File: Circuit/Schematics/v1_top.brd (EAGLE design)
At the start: 31.5 x 31.5 mm, 42 parts, among them IC1 LM2936MP-3.3, X2 16 Mhz, X3 16 Mhz

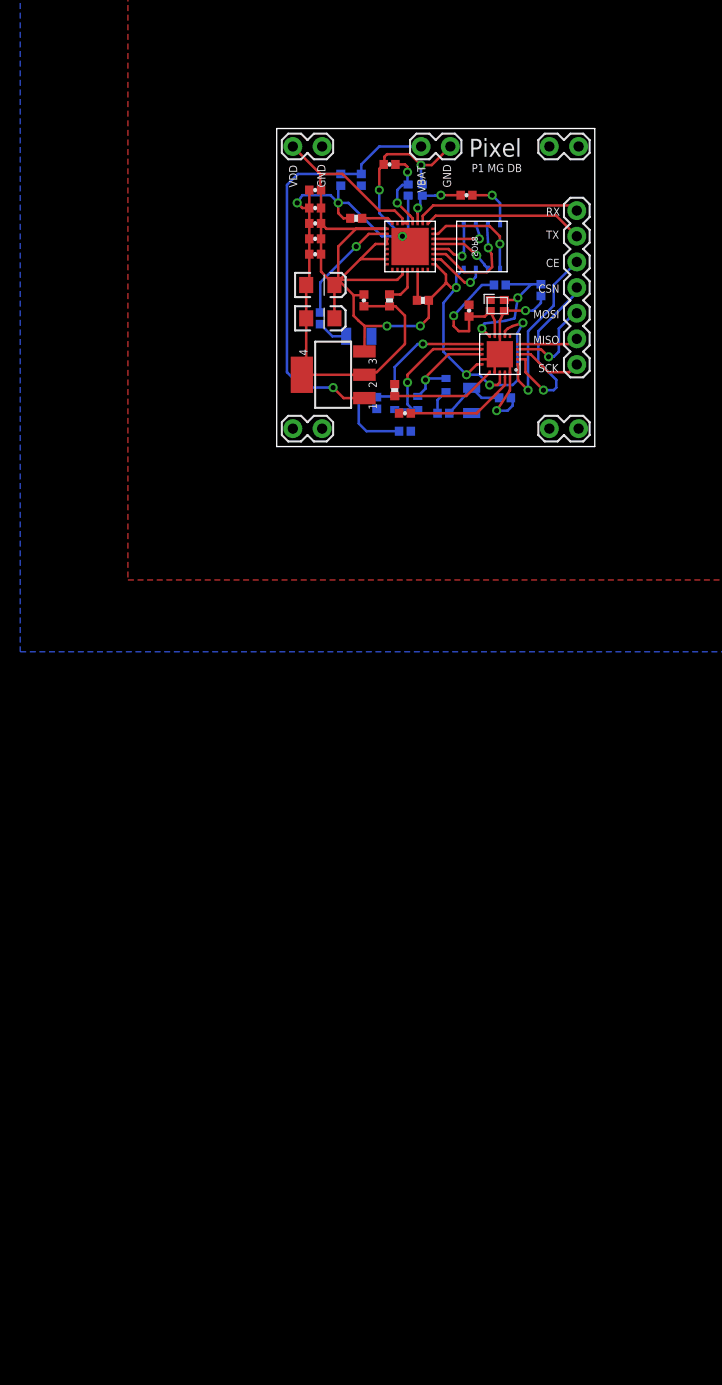
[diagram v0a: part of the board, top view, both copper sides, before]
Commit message: Teensy board designed, redesigning system components board and making hardware components consistent
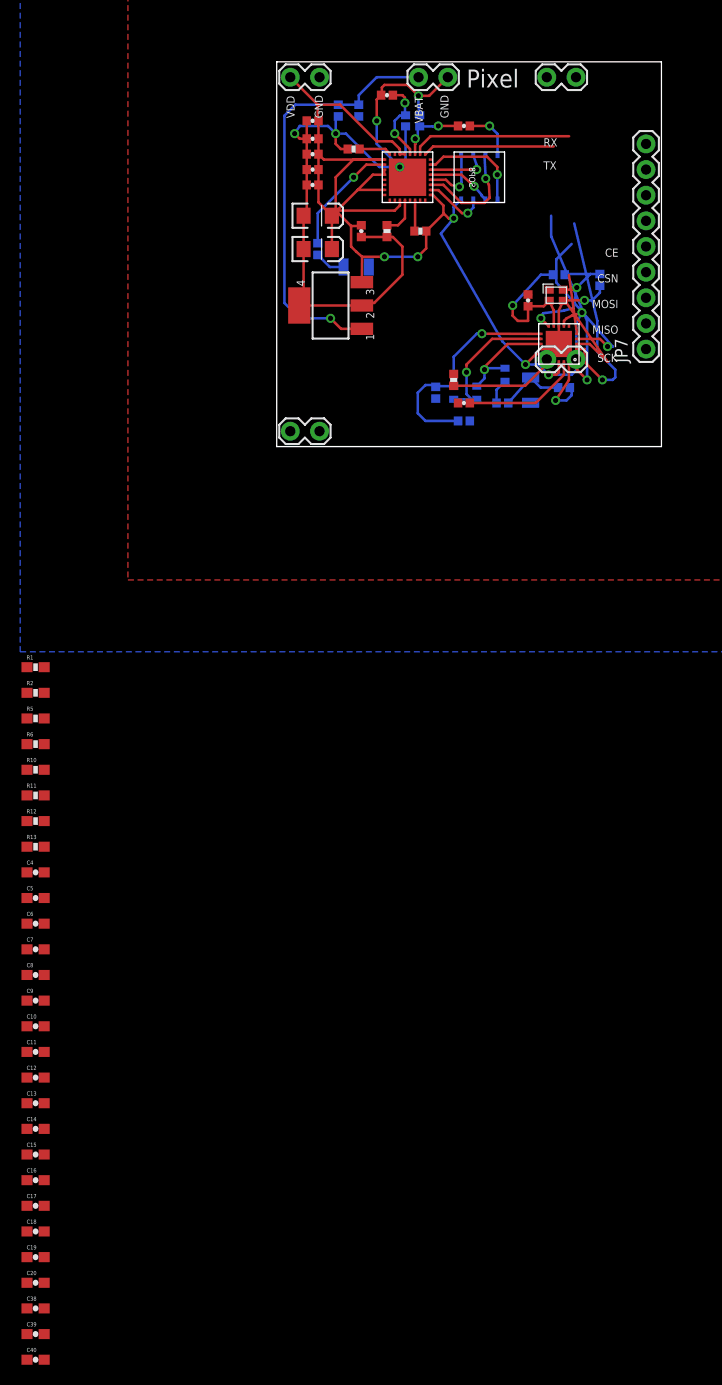
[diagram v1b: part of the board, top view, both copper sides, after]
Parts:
- removed JP1: (no value), SparkFun-Connectors:1X07
- added C10, C11, C12, C13, C14, C15, C16, C17, C18, C19, C20, C38, C39, C4, C40, C5, C6, C7, C8, C9: (no value), SparkFun-Capacitors:0603-CAP
- added JP7: (no value), SparkFun-Connectors:1X09
- added R1, R10, R11, R12, R13, R2, R5, R6: (no value), SparkFun-Resistors:0603-RES
- moved C27 6.86 mm to (3.56, 32.3)
- moved X3 6.86 mm to (13.5, 32.3)
- moved C1 6.86 mm to (8.13, 33.3)
- moved C2 6.86 mm to (4.06, 22.9)
- moved C21 6.86 mm to (4.06, 19.6)
- moved C23 6.86 mm to (10.9, 34.8)
- moved C24 6.86 mm to (18.5, 31.8)
- moved C25 6.86 mm to (6.10, 33.3)
- moved C26 6.86 mm to (3.56, 25.9)
- moved C28 6.86 mm to (3.56, 29.0)
- moved C3 6.86 mm to (4.06, 19.6)
- moved C30 6.86 mm to (3.56, 30.5)
- moved IC1 6.86 mm to (5.33, 14.0)
- moved JP2 6.86 mm to (1.52, 36.6)
- moved JP5 6.86 mm to (26.9, 36.6)
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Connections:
- new net SCL: JP7.9
- new net SDA: JP7.8
- net CE: now also JP7.3; no longer JP1.3
- net CSN: now also JP7.4; no longer JP1.4
- net MISO: now also JP7.6; no longer JP1.6
- net MOSI: now also JP7.5; no longer JP1.5
- net RX_W: now also JP7.1; no longer JP1.1
- net SCK: now also JP7.7; no longer JP1.7
- net TX_W: now also JP7.2; no longer JP1.2
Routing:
- net MOSI: track 9.26 -> 16.7 mm
- net VDD: track 116.4 -> 123.8 mm
- net CSN: track 18.1 -> 22.1 mm
- net SCK: track 6.87 -> 10.9 mm
- net TX_W: track 15.9 -> 13.0 mm
- net CE: track 17.7 -> 19.9 mm
- net RX_W: track 16.6 -> 15.9 mm
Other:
- board size 31.5 x 31.5 mm -> 38.1 x 38.1 mm
- board text removed: "P1 MG DB"

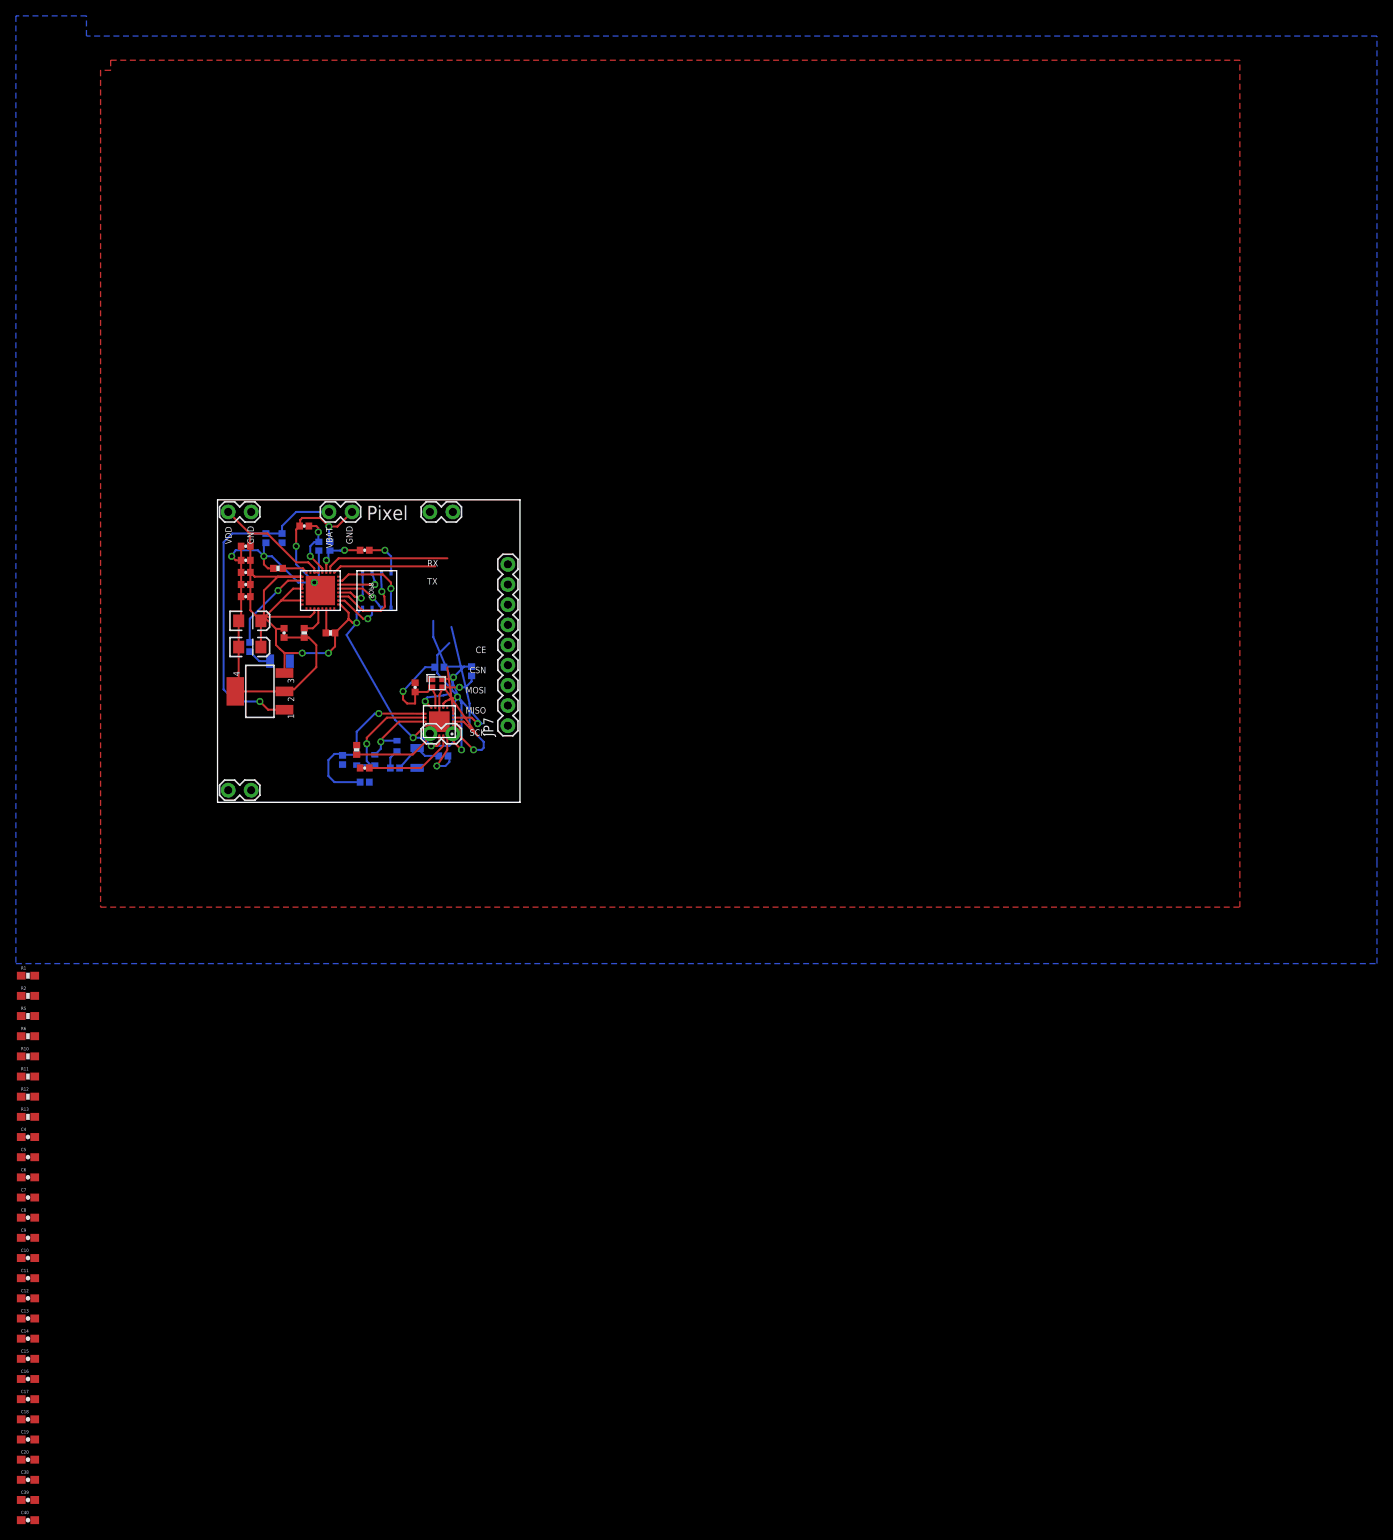
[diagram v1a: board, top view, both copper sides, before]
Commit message: System components board almost done. Final tweaking
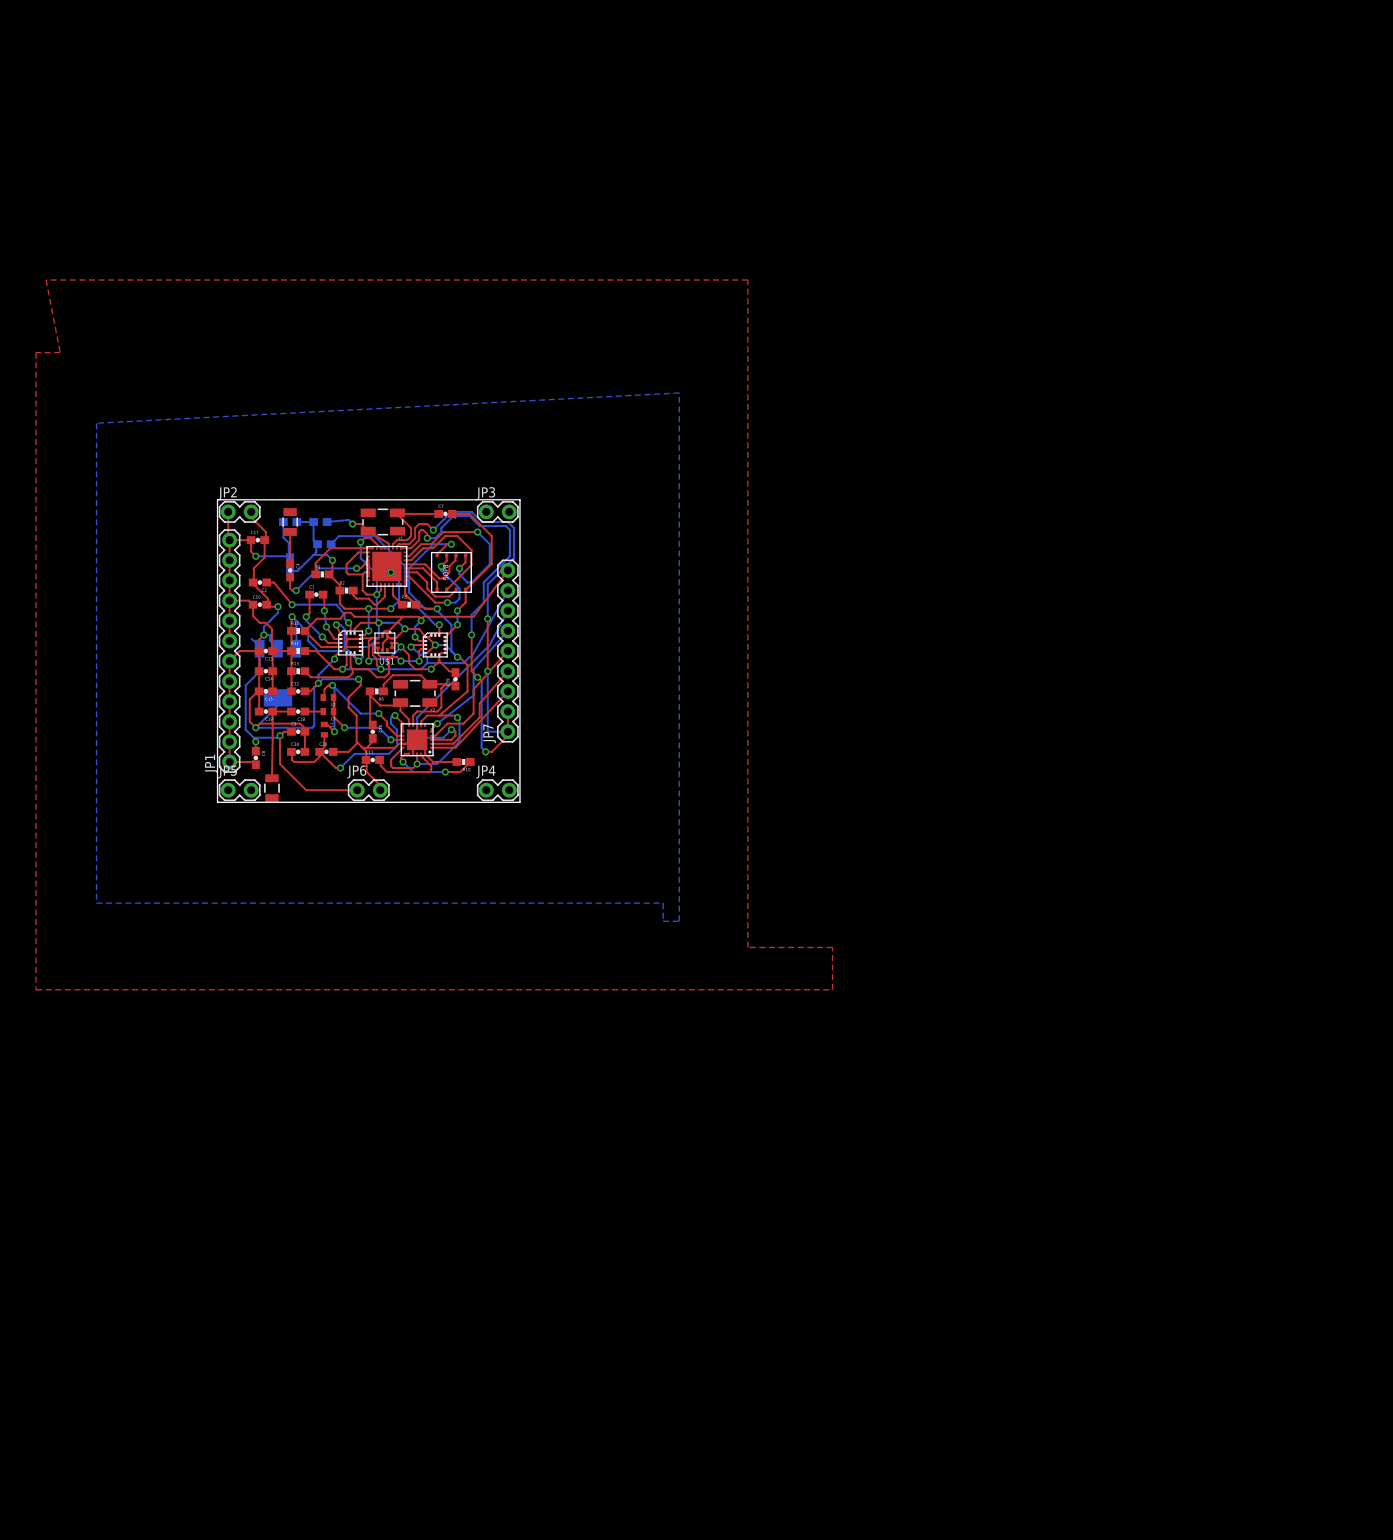
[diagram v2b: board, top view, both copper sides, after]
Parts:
- removed C21: 5.6 pF, SparkFun-Capacitors:0402-CAP
- removed C22, C26: 1 uF, SparkFun-Capacitors:0402-CAP
- removed C23, C24: 15 pF, SparkFun-Capacitors:0402-CAP
- removed C25, C27, C28, C29, C30: .1 uF, SparkFun-Capacitors:0402-CAP
- removed C31: 33 nF, SparkFun-Capacitors:0402-CAP
- removed C32: 1.5 pF, SparkFun-Capacitors:0402-CAP
- removed C33: 1.0 pF, SparkFun-Capacitors:0402-CAP
- removed C34: 2.2 nF, SparkFun-Capacitors:0402-CAP
- removed C35: 4.7 pF, SparkFun-Capacitors:0402-CAP
- removed C36, C37: 22 pF, SparkFun-Capacitors:0402-CAP
- removed R3, R7, R8: 12k, SparkFun-Resistors:0402-RES
- removed R4: 22k, SparkFun-Resistors:0402-RES
- removed R9: 1M, SparkFun-Resistors:0402-RES
- removed X2, X3: 16 Mhz, crystals:TXC-8Y
- added JP1: (no value), SparkFun-Connectors:1X12
- added U$1: LPS25H, chips:LPS25H
- added U$2: LSM303D, st:LGA16L
- added U$3: L3GD20H, st:LGA16L
- added Y1, Y2: 16 Mhz, SparkFun-FreqCtrl:CRYSTAL-SMD-5X3
- C1: value 1 uF -> .22 uF; device SparkFun-Capacitors:0402-CAP -> SparkFun-Capacitors:0603-CAP
- C10: value (none) -> 10 uF
- C11: value (none) -> 33 nF
- C12: value (none) -> 4.7 uF
- C13, C5, C8: value (none) -> 1 uF
- C14, C15, C16, C17, C9: value (none) -> .1 uF
- C18: value (none) -> 1.5 pF
- C19: value (none) -> 1.0 pF
- C2: value 10 uF -> 4.7 uF; device SparkFun-Capacitors:EIA3216 -> SparkFun-Capacitors:0603-CAP
- C20: value (none) -> 2.2 nF
- C3: value 4.7 uF -> 10 nF; device SparkFun-Capacitors:EIA3216 -> SparkFun-Capacitors:0603-CAP
- C38: value (none) -> 4.7 pF
- C39, C40: value (none) -> 22 pF
- C4: value (none) -> 5.6 pF
- C6, C7: value (none) -> 15 pF
- R1, R2, R5: value (none) -> 12k
- R10: value (none) -> 22k
- R6: value (none) -> 1M
- moved C39 116.6 mm to (30.0, 15.5), turned to 90 degrees
- moved C17 112.0 mm to (5.08, 33.0)
- moved C40 108.4 mm to (19.6, 8.89), turned to 270 degrees
- moved C16 107.8 mm to (9.14, 30.0), flipped to the bottom, turned to 270 degrees
- moved C7 100.9 mm to (28.7, 36.3)
- moved C38 97.8 mm to (10.2, 6.35)
- moved C20 96.8 mm to (13.7, 6.35)
- moved C19 96.5 mm to (6.10, 11.4), turned to 180 degrees
- moved C18 95.4 mm to (10.2, 11.4), turned to 180 degrees
- moved C6 90.4 mm to (13.0, 35.3), flipped to the bottom
- moved C13 89.3 mm to (6.10, 19.1), turned to 180 degrees
- moved C14 89.3 mm to (6.10, 16.5), turned to 180 degrees
- moved C15 89.3 mm to (6.10, 14.0), turned to 180 degrees
- moved C10 87.3 mm to (5.33, 24.9)
- moved C5 86.6 mm to (9.14, 35.3), flipped to the bottom
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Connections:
- removed net N$12: R7.2, WIFI.MTCK/12
- new net N$14: U$1.7
- new net N$3: R2.2, WIFI.MTCK/12
- new net N$35: U$2.P$11
- new net N$36: U$2.P$9
- new net N$42: C1.2, U$2.P$2
- new net N$43: C2.1, U$2.P$15
- new net N$49: U$3.P$7
- new net N$50: U$3.P$6
- new net N$54: C3.1, U$3.P$14
- new net N$58: U$3.P$15
- new net SDO: R13.2, U$1.5, U$2.P$7, U$3.P$4
- new net SETP: C1.1, U$2.P$3
- net GND: now also C10.2, C11.1, C12.2, C13.2, C14.2, C15.2, C16.2, C17.2, C19.2, C2.2, C20.2, C3.2, C38.2, C39.2, C40.2, C5.1, C6.2, C7.2, C8.2, C9.2, JP1.1, JP1.2, JP1.3, JP1.4, JP1.5, JP1.6, R1.2, R10.2, R2.1, U$1.3, U$1.8, U$1.9, U$2.P$10, U$2.P$12, U$2.P$13, U$2.P$16, U$2.P$5, U$3.P$10, U$3.P$11, U$3.P$12, U$3.P$13, U$3.P$8, U$3.P$9; no longer C1.2, C2.C, C22.1, C23.2, C24.2, C25.2, C26.2, C27.2, C28.2, C29.2, C3.C, C30.2, C31.1, C33.2, C34.2, C35.2, C36.2, C37.2, R4.2, R7.1, R8.2, X2.2, X2.4, X3.2, X3.4
- net N$1: now also C4.1; no longer C21.1
- net N$10: now also C18.2, C19.1; no longer C32.2, C33.1
- net N$13: now also C4.2; no longer C21.2
- net N$16: now also C39.1, R6.1, Y2.1; no longer C36.1, R9.1, X2.1
- net N$17: now also C40.1, R6.2, Y2.3; no longer C37.1, R9.2, X2.3
- net N$18: now also C20.1, C38.1; no longer C34.1, C35.1
- net N$2: now also R5.1; no longer R3.1
- net N$24: now also R10.1; no longer R4.1
- net N$28: now also C11.2; no longer C31.2
- net N$6: now also C18.1; no longer C32.1
- net RST: now also R1.1; no longer R8.1
- net SCL: now also R12.2, U$1.2, U$2.P$4, U$3.P$2
- net SDA: now also R11.2, U$1.4, U$2.P$6, U$3.P$3
- net VDD: now also C10.1, C12.1, C13.1, C14.1, C15.1, C16.1, C17.1, C5.2, JP1.10, JP1.11, JP1.12, JP1.7, JP1.8, JP1.9, R11.1, R12.1, R13.1, R5.2, U$1.1, U$1.10, U$1.6, U$2.P$1, U$2.P$14, U$2.P$8, U$3.P$1, U$3.P$16, U$3.P$5; no longer C2.A, C22.2, C26.1, C27.1, C28.1, C29.1, C3.A, C30.1, R3.2
- net VRAW: now also C8.1, C9.1; no longer C1.1, C25.1
- net XTAL_IN: now also C6.1, Y1.3; no longer C23.1, X3.3
- net XTAL_OUT: now also C7.1, Y1.1; no longer C24.1, X3.1
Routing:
- net GND: track 107.5 -> 228.7 mm, vias 8 -> 16
- net VDD: track 123.8 -> 205.7 mm, vias 6 -> 14
- net SCL: track 0.00 -> 43.8 mm, vias 0 -> 2
- net SDA: track 0.00 -> 43.7 mm, vias 0 -> 3
- net TX_W: track 13.0 -> 55.6 mm, vias 0 -> 4
- net RX_W: track 15.9 -> 48.5 mm, vias 0 -> 3
- net SDO: track 0.00 -> 25.0 mm, vias 0 -> 2
- net N$54: track 0.00 -> 22.0 mm, vias 0 -> 1
- net SCK: track 10.9 -> 29.2 mm, vias 0 -> 1
- net N$43: track 0.00 -> 14.3 mm, vias 0 -> 2
- net SD-D1: track 10.6 -> 23.1 mm, vias 1 -> 2
- net MISO: track 5.90 -> 16.9 mm, vias 0 -> 1
- net SD-D0: track 6.05 -> 16.7 mm, vias 1 -> 0
- net SD-D2: track 6.19 -> 15.2 mm, vias 1 -> 2
- net SETP: track 0.00 -> 8.92 mm, vias 0 -> 2
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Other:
- board text removed: "CE"
- board text removed: "CSN"
- board text removed: "GND"
- board text removed: "MISO"
- board text removed: "MOSI"
- board text removed: "Pixel"
- board text removed: "RX"
- board text removed: "SCK"
- board text removed: "TX"
- board text removed: "VBAT"
- board text removed: "VDD"
